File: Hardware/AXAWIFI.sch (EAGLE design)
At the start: 25 parts, among them IC1 MCP2003, J1 ESPROG-SOCKET, SW1 RESET, SW2 REFLASH

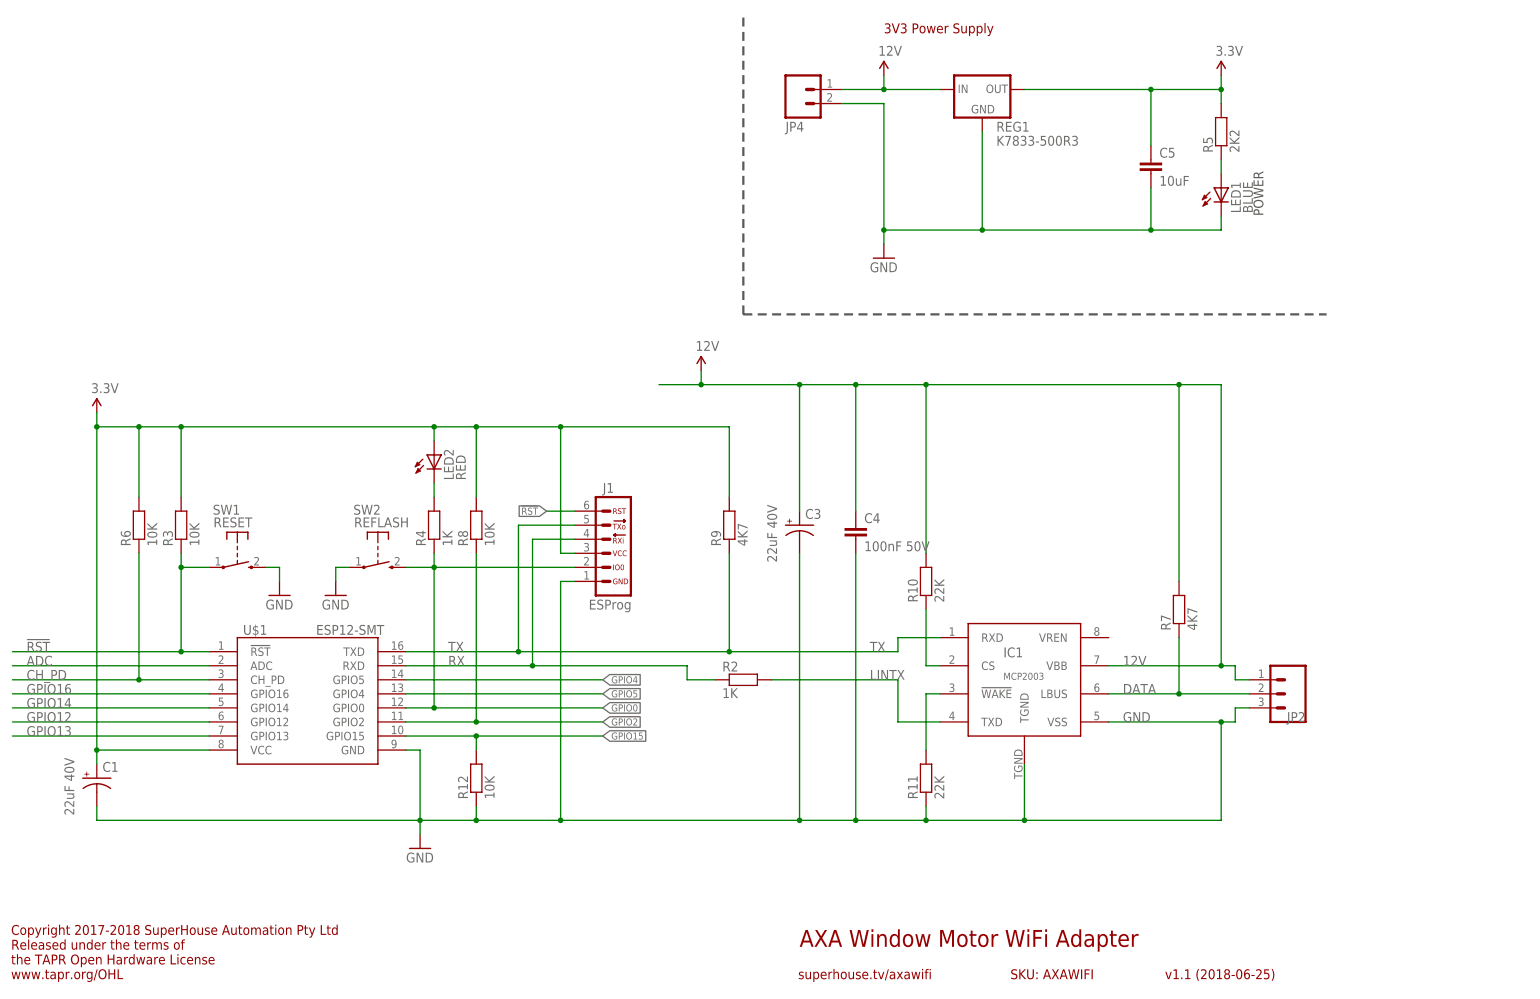
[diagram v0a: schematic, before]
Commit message: Replaced obsolete programming header with ESPFlash header. Set MCP2003 to be permanently awake. Set MCP2003 to be deselected unless explicitly selected. Major restructure of schematic. Replaced parts using latest SuperHouse Eagle libraries to add 3D models.
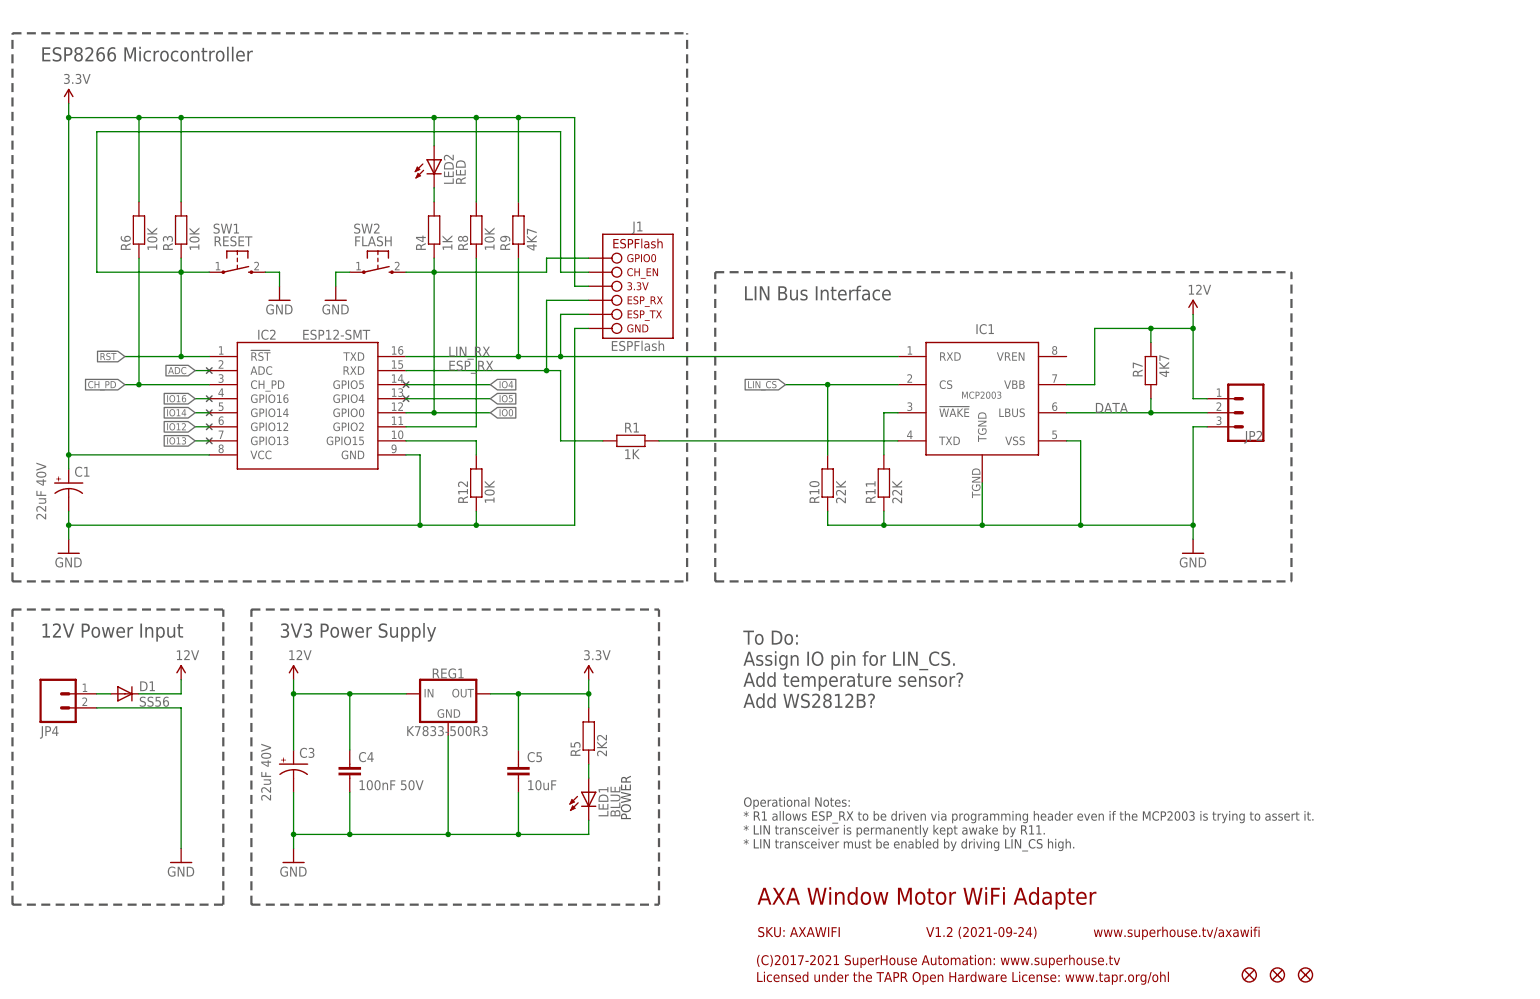
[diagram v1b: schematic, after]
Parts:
- removed R2: 1K, SuperHouse-DiscreteSemi:RESISTOR0603
- removed U$1: ESP12-SMT, SuperHouse-MCUs:ESP12-SMT
- added D1: SS56, SuperHouse-Diodes:DIODESMA
- added FID1, FID2, FID3: FIDUCIAL1X2.5, SuperHouse-Symbols:FIDUCIAL1X2.5
- added IC2: ESP12-SMT, SuperHouse-MCUs:ESP12-SMT
- added R1: 1K, SuperHouse-Resistors:RESISTOR0603
- C1, C3: device SuperHouse-DiscreteSemi:CAP_POLC -> SuperHouse-Capacitors:CAP_POLC
- C4: device SuperHouse-DiscreteSemi:CAP0603 -> SuperHouse-Capacitors:CAP0603
- C5: device SuperHouse-DiscreteSemi:CAP0805 -> SuperHouse-Capacitors:CAP0805
- J1: value ESPROG-SOCKET -> ESPFLASH-1X6-2.54-SOCKET; device SuperHouse-Connectors:ESPROG-SOCKET -> SuperHouse-ESPFlash:ESPFLASH-1X6-2.54-SOCKET
- R10, R11, R12, R3, R4, R5, R6, R7, R8, R9: device SuperHouse-DiscreteSemi:RESISTOR0603 -> SuperHouse-Resistors:RESISTOR0603
- REG1: device SuperHouse-Regulators:K78XX-500R3 -> SuperHouse-Regulators:78XX-K78XX-VERTICAL
- SW2: value REFLASH -> FLASH
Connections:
- net N$6 renamed !LIN_WAKE
- removed net GPIO0: J1.2, R4.1, SW2.S, U$1.GPIO0
- removed net GPIO12: U$1.GPIO12
- removed net GPIO13: U$1.GPIO13
- removed net GPIO14: U$1.GPIO14
- removed net GPIO16: U$1.GPIO16
- removed net GPIO4: U$1.GPIO5
- removed net GPIO5: U$1.GPIO4
- removed net LINTX: IC1.TXD, R2.2
- removed net N$5: IC1.CS, R10.1
- removed net RX: J1.4, R2.1, U$1.RXD
- removed net TX: IC1.RXD, J1.5, R9.1, U$1.TXD
- new net ESP_RX: IC2.RXD, J1.ESP_RX, R1.1
- new net IO0: IC2.GPIO0, J1.GPIO0, R4.1, SW2.S
- new net IO12: IC2.GPIO12
- new net IO13: IC2.GPIO13
- new net IO14: IC2.GPIO14
- new net IO16: IC2.GPIO16
- new net IO4: IC2.GPIO5
- new net IO5: IC2.GPIO4
- new net LIN_CS: IC1.CS, R10.2
- new net LIN_RX: IC1.RXD, IC2.TXD, J1.ESP_TX, R9.1
- new net N$1: D1.A, JP4.1
- new net N$2: IC1.TXD, R1.2
- net !RST: now also IC2.!RST, J1.CH_EN; no longer J1.6, U$1.!RST
- net 12V: now also D1.C; no longer JP4.1, R10.2
- net 3.3V: now also IC2.VCC, J1.3.3V; no longer J1.3, U$1.VCC
- net ADC: now also IC2.ADC; no longer U$1.ADC
- net CH_PD: now also IC2.CH_PD; no longer U$1.CH_PD
- net GND: now also IC2.GND, J1.GND, R10.1; no longer J1.1, U$1.GND
- net GPIO15: now also IC2.GPIO15; no longer U$1.GPIO15
- net GPIO2: now also IC2.GPIO2; no longer U$1.GPIO2
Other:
- note added: "(C)2017-2021 SuperHouse Automation: www.superhouse.tv"
- note added: "12V Power Input"
- note added: "ESP8266 Microcontroller"
- note added: "LIN Bus Interface"
- note added: "Licensed under the TAPR Open Hardware License: www.tapr.org/ohl"
- note added: "Operational Notes: * R1 allows ESP_RX to be driven via programming header even if the MCP2003 is trying to assert it. * LIN transceiver is permanently kept awake by R11. * LIN transceiver must be enabled by driving LIN_CS high."
- note added: "To Do: Assign IO pin for LIN_CS. Add temperature sensor? Add WS2812B?"
- note added: "V1.2 (2021-09-24)"
- note added: "www.superhouse.tv/axawifi"
- note removed: "Copyright 2017-2018 SuperHouse Automation Pty Ltd Released under the terms of the TAPR Open Hardware License www.tapr.org/OHL"
- note removed: "superhouse.tv/axawifi"
- note removed: "v1.1 (2018-06-25)"
- moved on the sheet: C1, C3, C4, C5, IC1, JP2, JP4, LED1, LED2, R10, R11, R12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

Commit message: Assigned IO15 as LIN_CS.
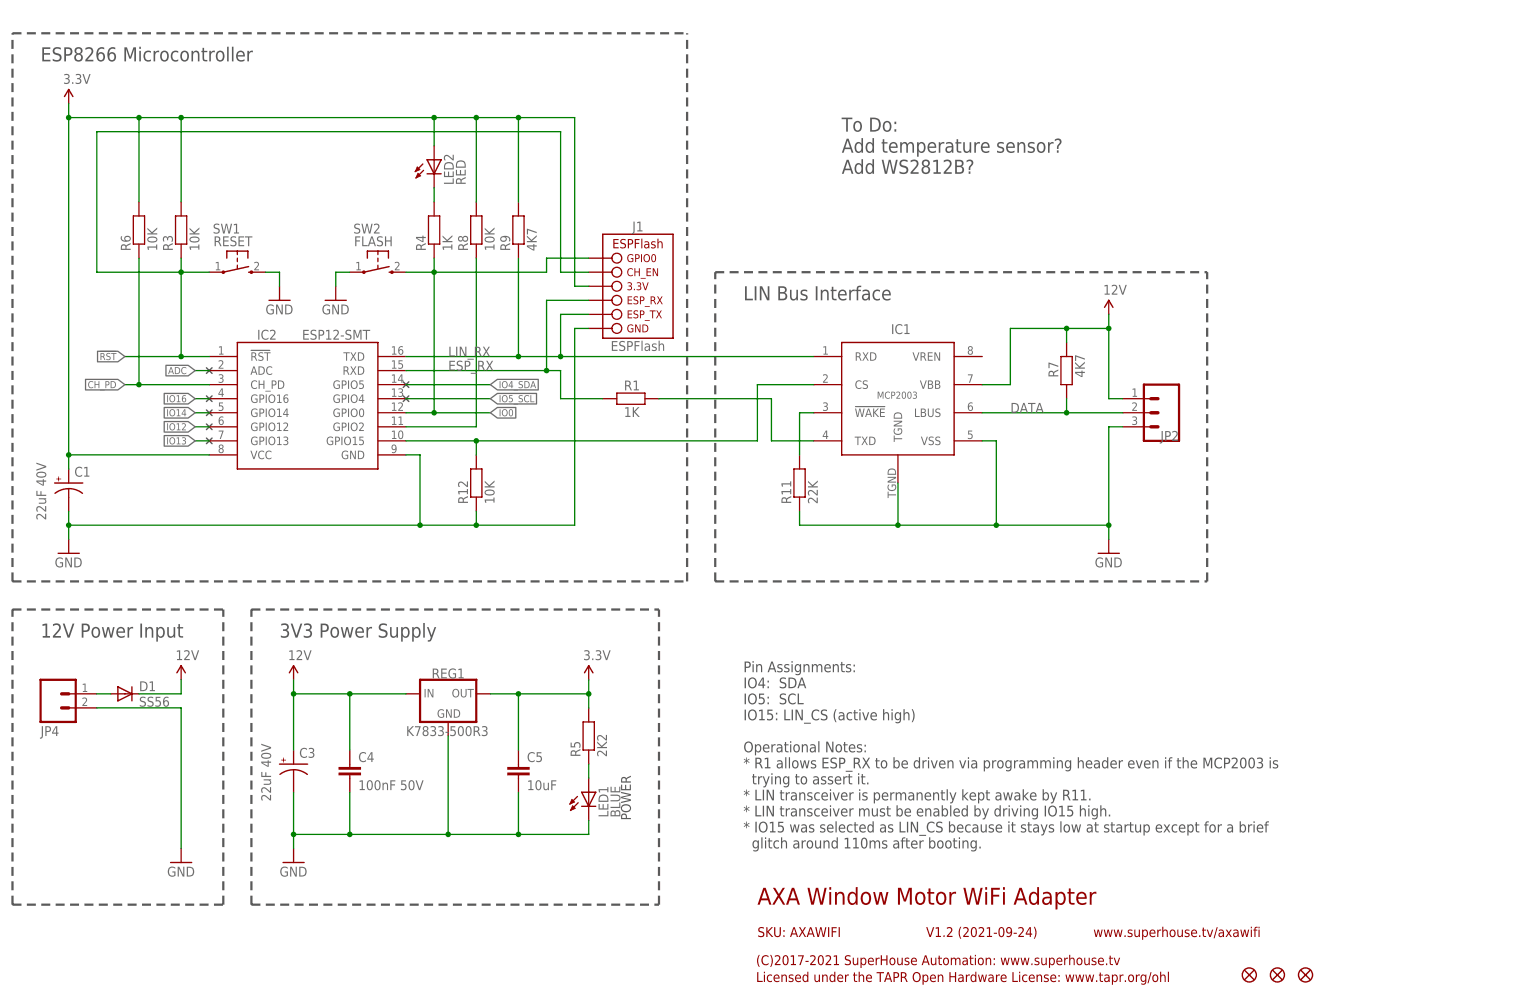
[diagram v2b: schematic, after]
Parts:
- removed R10: 22K, SuperHouse-Resistors:RESISTOR0603
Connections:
- net IO4 renamed IO4_SDA
- net IO5 renamed IO5_SCL
- removed net LIN_CS: IC1.CS, R10.2
- net GND: no longer R10.1
- net GPIO15: now also IC1.CS
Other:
- note added: "Pin Assignments: IO4: SDA IO5: SCL IO15: LIN_CS (active high) Operational Notes: * R1 allows ESP_RX to be driven via programming header even if the MCP2003 is trying to assert it. * LIN transceiver is permanently kept awake by R11. * LIN transceiver must be enabled by driving IO15 high. * IO15 was selected as LIN_CS because it stays low at startup except for a brief glitch around 110ms after boot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"
- note added: "To Do: Add temperature sensor? Add WS2812B?"
- note removed: "Operational Notes: * R1 allows ESP_RX to be driven via programming header even if the MCP2003 is trying to assert it. * LIN transceiver is permanently kept awake by R11. * LIN transceiver must be enabled by driving LIN_CS high."
- note removed: "To Do: Assign IO pin for LIN_CS. Add temperature sensor? Add WS2812B?"
- moved on the sheet: IC1, JP2, R1, R11, R7

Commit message: Rationalised part values and reordered designators.
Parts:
- added IC3: MCP9808-MSOP8, SuperHouse-Sensors:MCP9808-MSOP8
- added LED3: GREEN, SuperHouse-LEDs:LED0603
- added R10: 10K, SuperHouse-Resistors:RESISTOR0603
- added R2: 1K, SuperHouse-Resistors:RESISTOR0603
- C1: value 22uF 40V -> 100nF 50V; device SuperHouse-Capacitors:CAP_POLC -> SuperHouse-Capacitors:CAP0603
- C4: value 100nF 50V -> 22uF 40V; device SuperHouse-Capacitors:CAP0603 -> SuperHouse-Capacitors:CAP_POLC
- R11: value 22K -> 10K
- R3: value 10K -> 1K
- R4: value 1K -> 2K2
- R5: value 2K2 -> 4K7
- R6, R8: value 10K -> 4K7
- R9: value 4K7 -> 10K
- renumbered C5 to C2
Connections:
- new net N$3: LED3.C, R3.2
- net !RST: now also R10.1; no longer R3.1
- net 12V: now also C1.1, R5.2; no longer C4.1, R7.2
- net 3.3V: now also C4.+, IC3.VDD, LED3.A, R10.2, R4.2, R7.2; no longer C1.+, R3.2, R5.2
- net CH_PD: now also R9.1; no longer R6.1
- net DATA: now also R5.1; no longer R7.1
- net GND: now also C1.2, C4.-, IC3.A0, IC3.A1, IC3.A2, IC3.GND; no longer C1.-, C4.2
- net GPIO2: now also R3.1; no longer R8.1
- net IO0: now also R2.1; no longer R4.1
- net IO4_SDA: now also IC3.SDA, R8.1
- net IO5_SCL: now also IC3.SCL, R7.1
- net LIN_RX: now also R6.1; no longer R9.1
- net N$14: now also R4.1; no longer R5.1
- net N$20: now also R2.2; no longer R4.2
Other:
- note added: "Bootloader"
- note added: "Pin Assignments: IO2: Status LED (active low) IO4: SDA IO5: SCL IO15: LIN_CS (active high) Operational Notes: * R1 allows ESP_RX to be driven via programming header even if the MCP2003 is trying to assert it. * The status LED doubles up as a pullup on the IO2 strapping pin. * LIN transceiver is permanently kept awake by R11. * LIN transceiver must be enabled by driving IO15 high. * IO15 was selec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"
- note added: "Power"
- note added: "Status"
- note added: "Temperature Sensor"
- note removed: "POWER"
- note removed: "Pin Assignments: IO4: SDA IO5: SCL IO15: LIN_CS (active high) Operational Notes: * R1 allows ESP_RX to be driven via programming header even if the MCP2003 is trying to assert it. * LIN transceiver is permanently kept awake by R11. * LIN transceiver must be enabled by driving IO15 high. * IO15 was selected as LIN_CS because it stays low at startup except for a brief glitch around 110ms after boot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"
- note removed: "To Do: Add temperature sensor? Add WS2812B?"
- moved on the sheet: IC1, J1, JP2, R1, R11, R3, R4, R5, R6, R7, R8, R9
